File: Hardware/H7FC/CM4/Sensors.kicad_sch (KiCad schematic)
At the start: 33 parts, among them J10 Conn_01x04, J11 Conn_01x06, J12 TSW-101-08-G-T-RA, J16 Conn_01x03_Female, J5 TSW-101-08-G-T-RA, J6 TSW-101-08-G-T-RA, J7 TSW-101-08-G-T-RA, J8 TSW-101-08-G-T-RA, J9 Conn_01x02, Q2 BC817W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

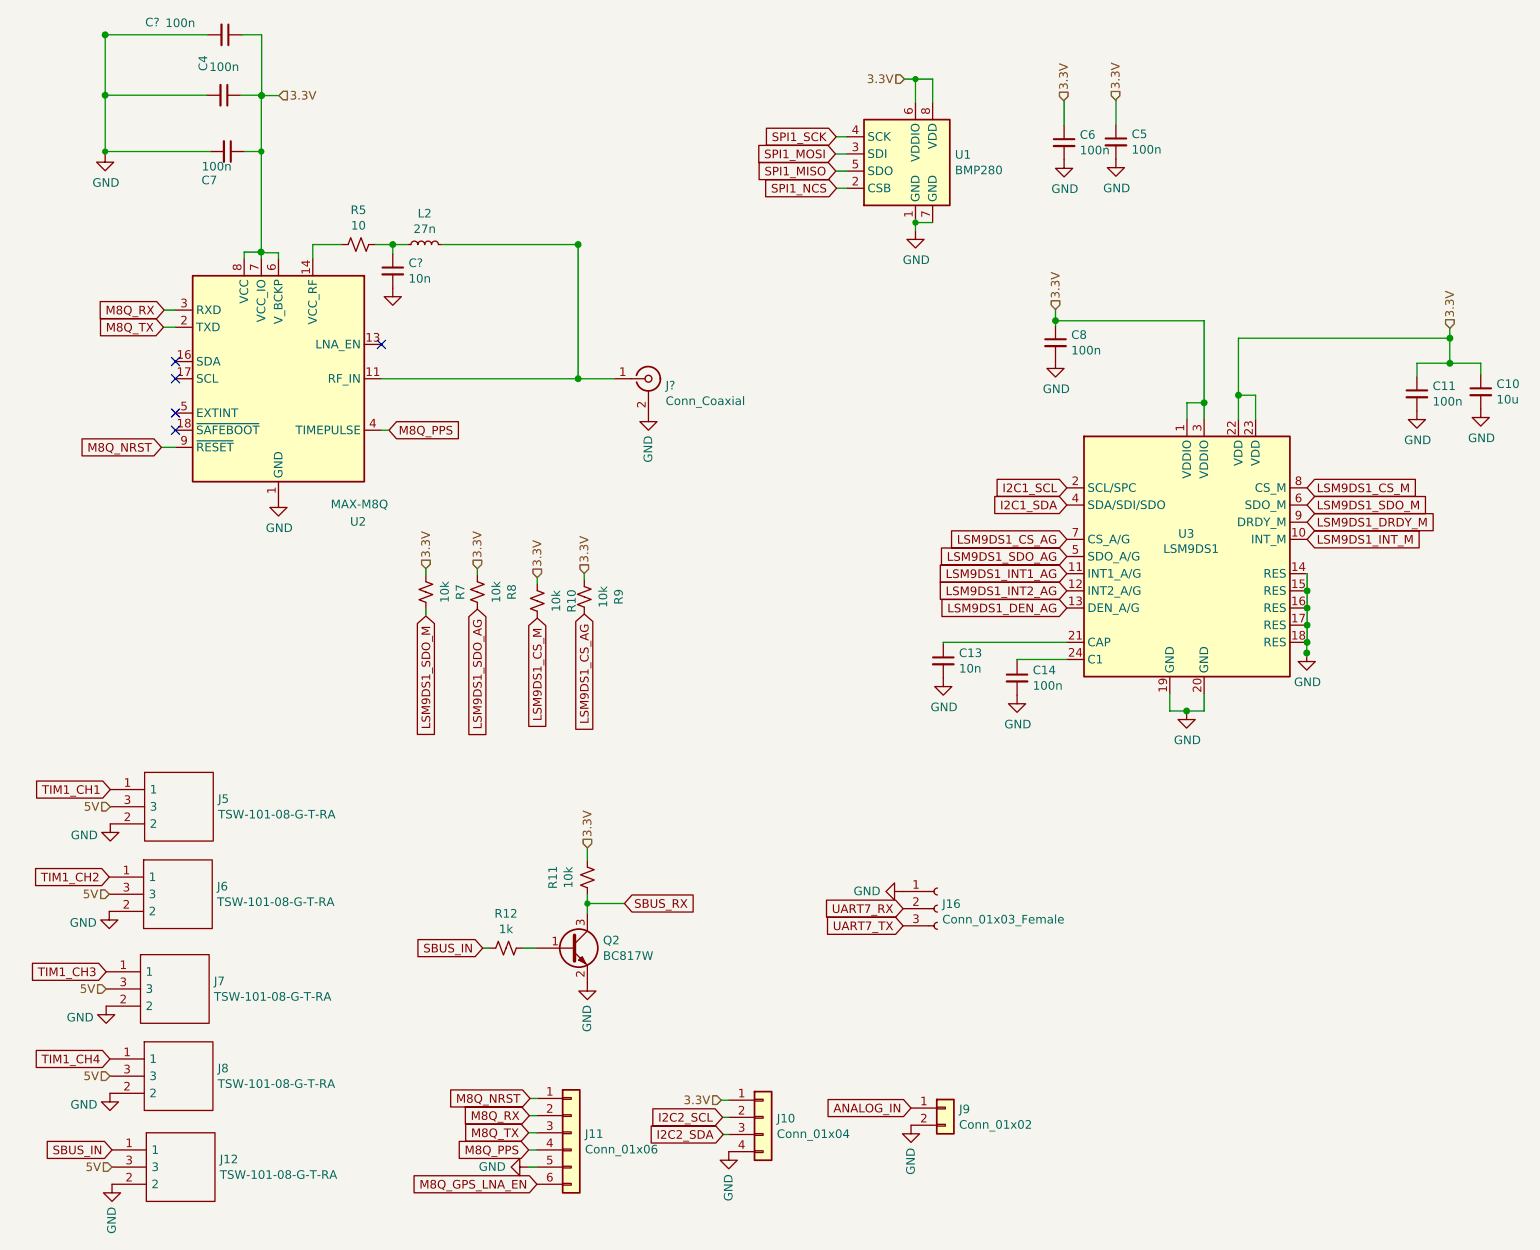
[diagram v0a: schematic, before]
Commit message: Set initial cUbeMX Cconfig. Fixed Clock and GPIO bug
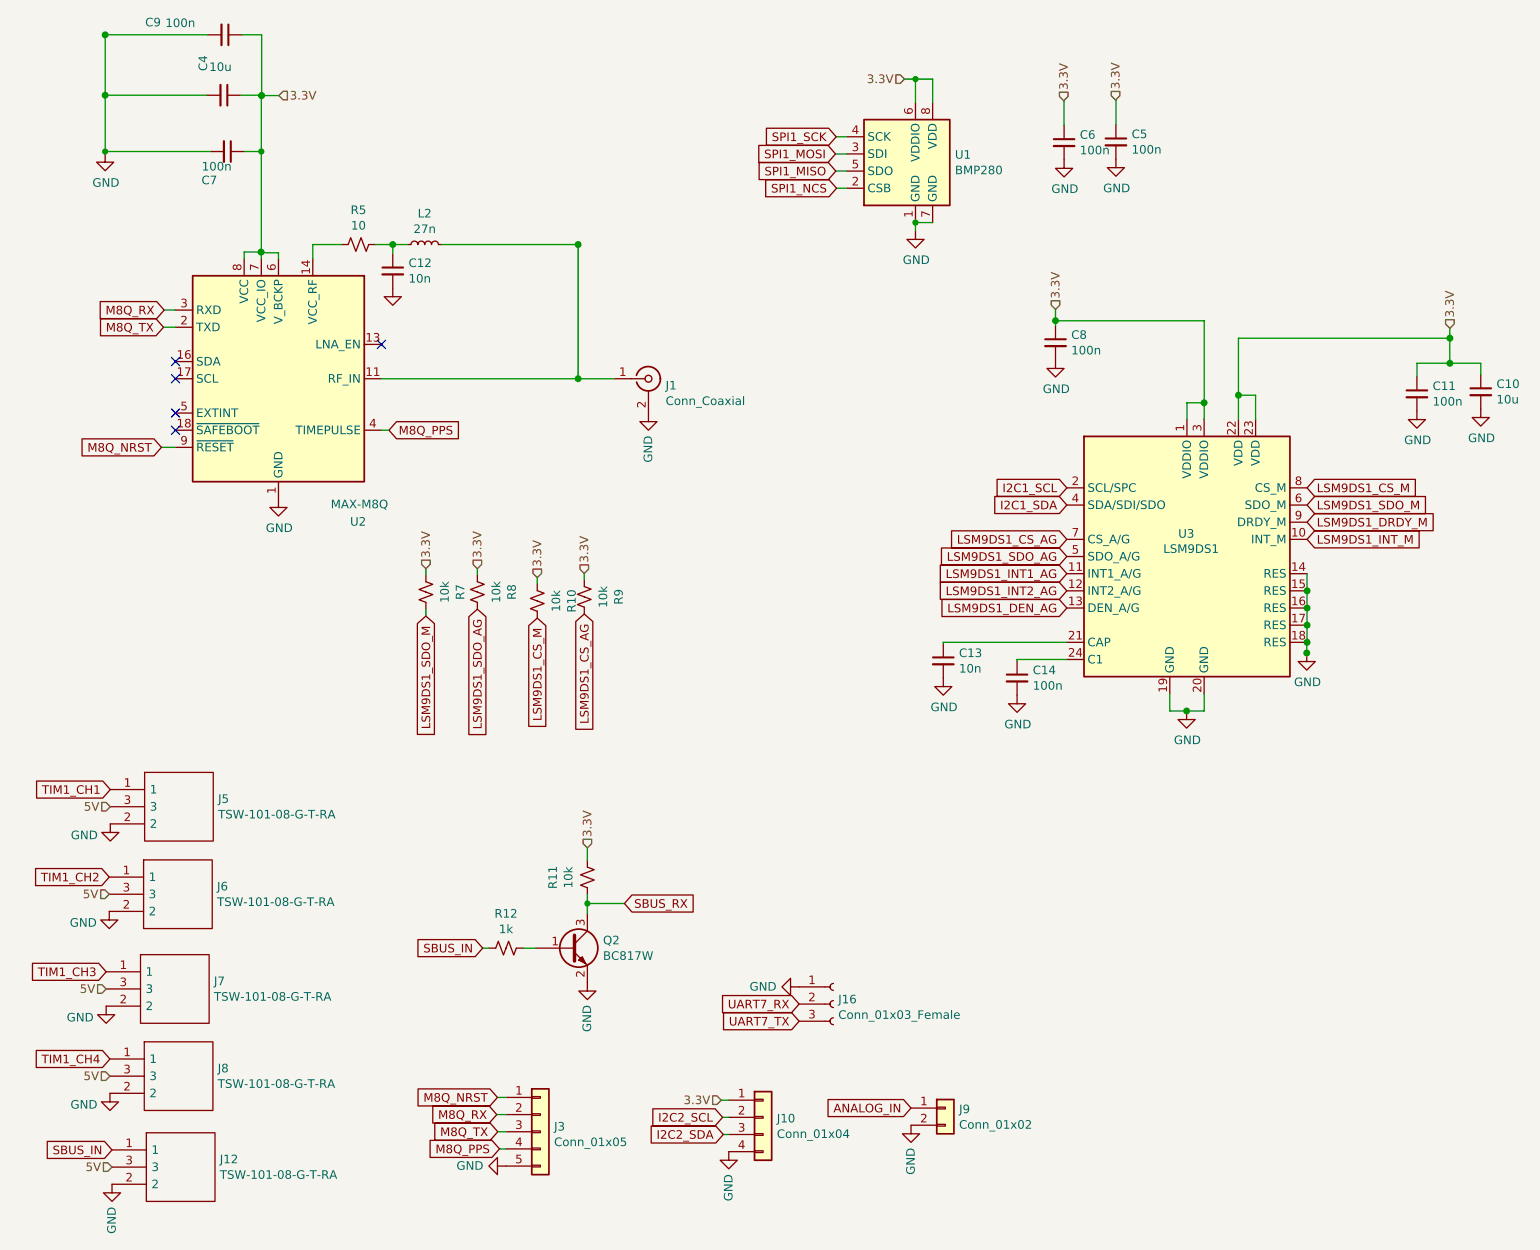
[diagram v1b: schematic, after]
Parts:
- removed J11: Conn_01x06, Connector_Molex:Molex_PicoBlade_53261-0671_1x06-1MP_P1.25mm_Horizontal, symbol Connector_Generic:Conn_01x06
- added J3: Conn_01x05, Connector_Molex:Molex_PicoBlade_53047-0510_1x05_P1.25mm_Vertical, symbol Connector_Generic:Conn_01x05
- C4: value 100n -> 10u
- J1: renamed from J?; footprint (none) -> CM4IO:BWIPX-1-001E
- J12, J5, J6, J7, J8: footprint HDRRA3W64P254_3X1_254X254X810P -> SamacSys_Parts:HDRRA3W64P254_3X1_254X254X810P
- gave numbers to parts that had none: 2
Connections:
- net GND: now also J3.5 (Pin_5)
- net M8Q_NRST: now also J3.1 (Pin_1)
- net M8Q_PPS: now also J3.4 (Pin_4)
- net M8Q_RX: now also J3.2 (Pin_2)
- net M8Q_TX: now also J3.3 (Pin_3)
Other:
- moved on the sheet: J16
